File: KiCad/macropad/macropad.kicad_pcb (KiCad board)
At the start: 2 copper layers, 124.5 x 57 mm, 24 parts, among them J1 Conn_01x06, SW1 SW_DIP_x01, SW2 SW_DIP_x01, SW3 SW_DIP_x01, SW4 SW_DIP_x01, SW5 SW_DIP_x01, SW6 SW_DIP_x01, U1 Pico

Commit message: Settings for gerber export
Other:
- outline, holes or cut-outs redrawn
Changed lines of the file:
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@@
       (layerselection 0x00010fc_ffffffff)
       (disableapertmacros false)
-      (usegerberextensions false)
-      (usegerberattributes true)
-      (usegerberadvancedattributes true)
-      (creategerberjobfile true)
+      (usegerberextensions true)
+      (usegerberattributes false)
+      (usegerberadvancedattributes false)
+      (creategerberjobfile false)
       (svguseinch false)
       (svgprecision 6)
@@
       (psa4output false)
       (plotreference true)
-      (plotvalue true)
+      (plotvalue false)
       (plotinvisibletext false)
       (sketchpadsonfab false)
-      (subtractmaskfromsilk false)
+      (subtractmaskfromsilk true)
       (outputformat 1)
       (mirror false)
-      (drillshape 1)
+      (drillshape 0)
       (scaleselection 1)
-      (outputdirectory "")
+      (outputdirectory "../macropad_gerber/")
     )
   )
@@
   )
   (gr_rect (start 174.5 53.5) (end 209.5 73.5) (layer "F.SilkS") (width 0.15) (fill none))
-  (gr_rect (start 105 21.5) (end 229.5 78.5) (layer "Edge.Cuts") (width 0.1) (fill none))
+  (gr_line (start 227.5 21.5) (end 107 21.5) (layer "Edge.Cuts") (width 0.1))
+  (gr_line (start 229.5 76.5) (end 229.5 23.5) (layer "Edge.Cuts") (width 0.1))
+  (gr_line (start 107 78.5) (end 227.5 78.5) (layer "Edge.Cuts") (width 0.1))
+  (gr_arc (start 227.5 21.5) (mid 228.914214 22.085786) (end 229.5 23.5) (layer "Edge.Cuts") (width 0.1))
+  (gr_arc (start 229.5 76.5) (mid 228.914214 77.914214) (end 227.5 78.5) (layer "Edge.Cuts") (width 0.1))
+  (gr_arc (start 107 78.5) (mid 105.585786 77.914214) (end 105 76.5) (layer "Edge.Cuts") (width 0.1))
+  (gr_arc (start 105 23.5) (mid 105.585786 22.085786) (end 107 21.5) (layer "Edge.Cuts") (width 0.1))
+  (gr_line (start 105 23.5) (end 105 76.5) (layer "Edge.Cuts") (width 0.1))
   (segment (start 113 33) (end 113 41.5) (width 0.25) (layer "F.Cu") (net 1))
   (segment (start 113 41.5) (end 114 42.5) (width 0.25) (layer "F.Cu") (net 1))

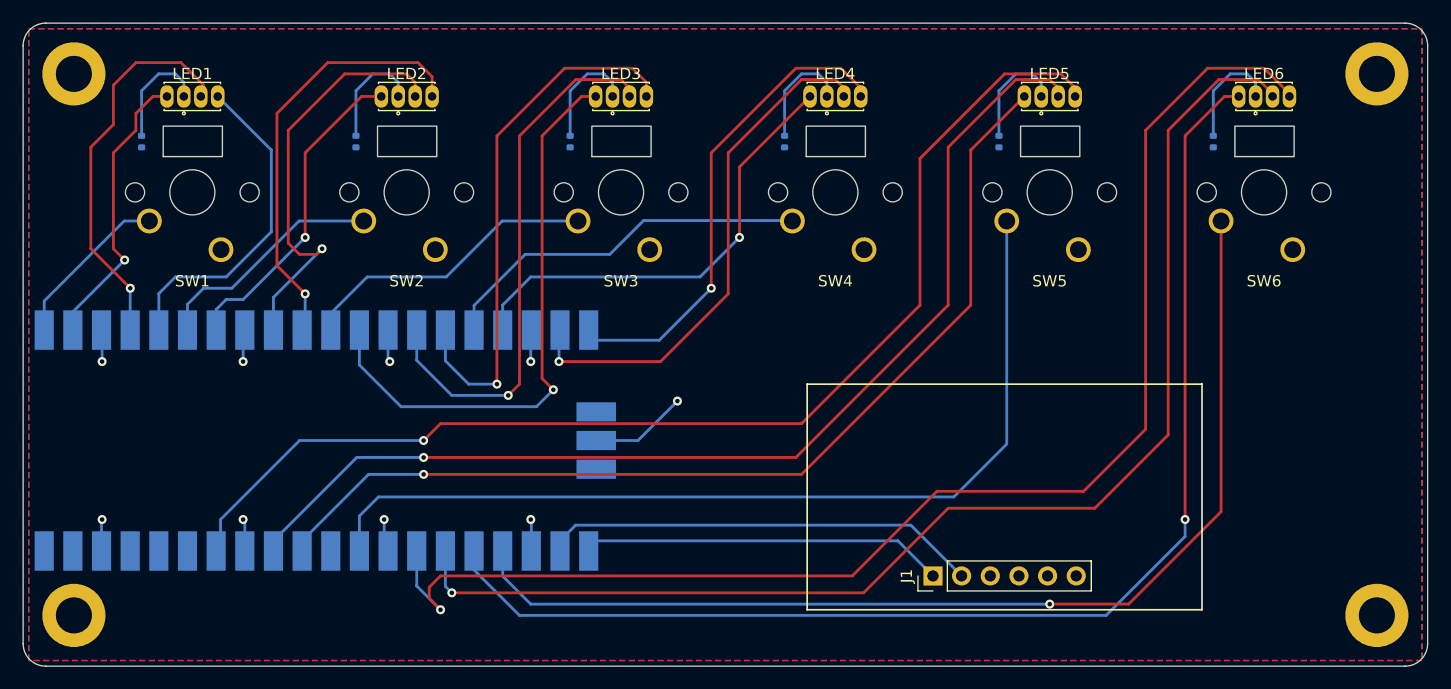
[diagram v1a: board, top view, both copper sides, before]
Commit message: Use THT resistors, correct Kailh key layout, giving up on this project for now in favor of streamdekc
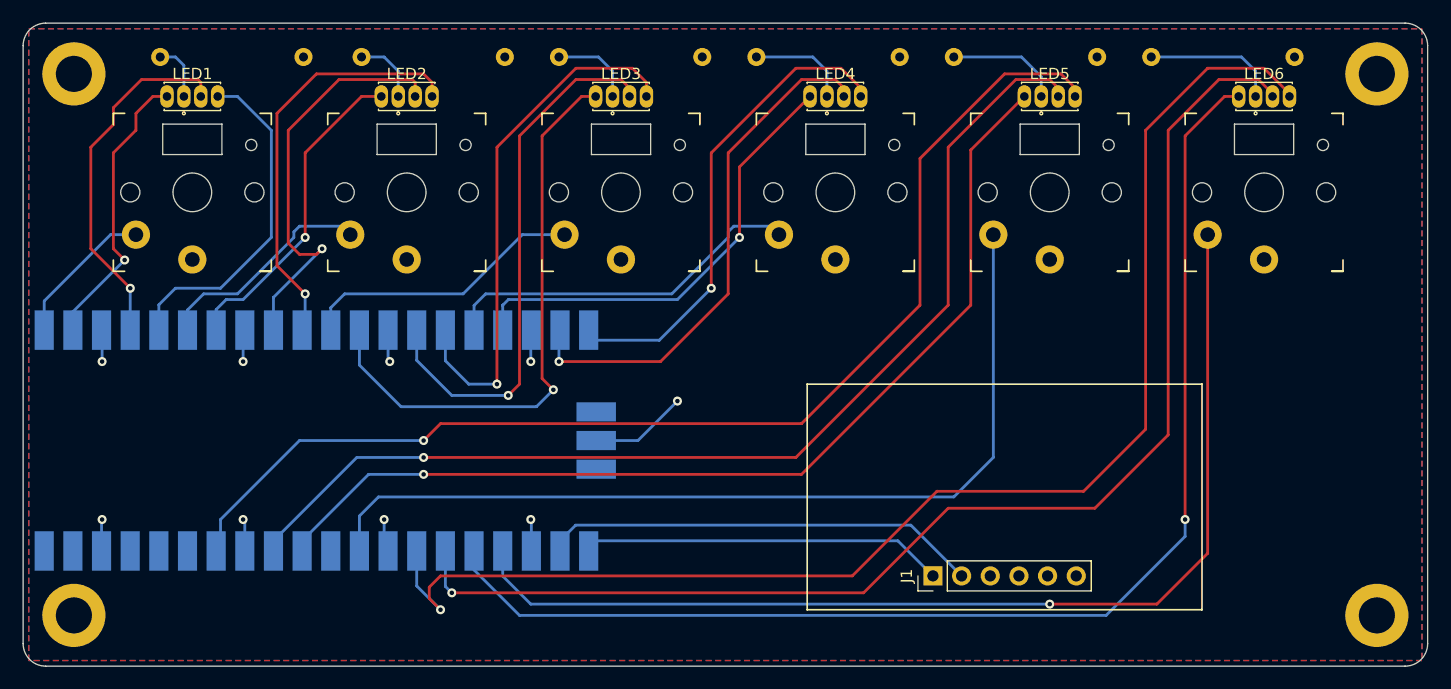
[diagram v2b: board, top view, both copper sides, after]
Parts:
- R1, R2, R3, R4, R5, R6: footprint Resistor_SMD:R_0402_1005Metric -> Resistor_THT:R_Axial_DIN0309_L9.0mm_D3.2mm_P12.70mm_Horizontal
- SW1, SW2, SW3, SW4, SW5, SW6: footprint Library:SW_Cherry_MX_1.00u_PCB_LEDHole -> Kailh Socket PG1350:Kailh_socket_PG1350; moved to F.Cu
- moved R1 16.2 mm to (129.8, 24.5), turned to 180 degrees
- moved R2 15.2 mm to (147.7, 24.5), turned to 180 degrees
- moved R3 13.9 mm to (165.2, 24.5), turned to 180 degrees
- moved R4 12.7 mm to (182.7, 24.5), turned to 180 degrees
- moved R5 11.5 mm to (200.2, 24.5), turned to 180 degrees
- moved R6 10.4 mm to (217.7, 24.5), turned to 180 degrees
- moved SW3 5.68 mm to (158.0, 36.5)
- moved SW1 5.68 mm to (120.0, 36.5)
- moved SW2 5.68 mm to (139.0, 36.5)
- moved SW4 5.68 mm to (177.0, 36.5)
- moved SW5 5.68 mm to (196.0, 36.5)
- moved SW6 5.68 mm to (215.0, 36.5)
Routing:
- net Net-(LED1-Pad4): track 9.92 -> 5.16 mm
- net Net-(LED2-Pad4): track 9.92 -> 6.02 mm
- net Net-(LED3-Pad4): track 9.93 -> 7.52 mm
- net Net-(LED6-Pad4): track 9.92 -> 12.0 mm
- net /LED1G: track 35.0 -> 33.0 mm
- net /BTN5: track 82.0 -> 80.3 mm
- net /BTN1: track 15.7 -> 14.0 mm
- net /BTN3: track 27.7 -> 26.3 mm
- net /LED2B: track 39.1 -> 38.0 mm
- net /BTN2: track 21.9 -> 20.8 mm
- net Net-(LED4-Pad4): track 9.92 -> 9.02 mm
- net /BTN4: track 34.4 -> 33.6 mm
- net /LED1B: track 30.3 -> 31.1 mm
- net /LED3B: track 46.8 -> 46.2 mm
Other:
- outline, holes or cut-outs redrawn
